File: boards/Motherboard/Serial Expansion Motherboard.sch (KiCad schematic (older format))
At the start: 5 parts, among them U401 24AA014

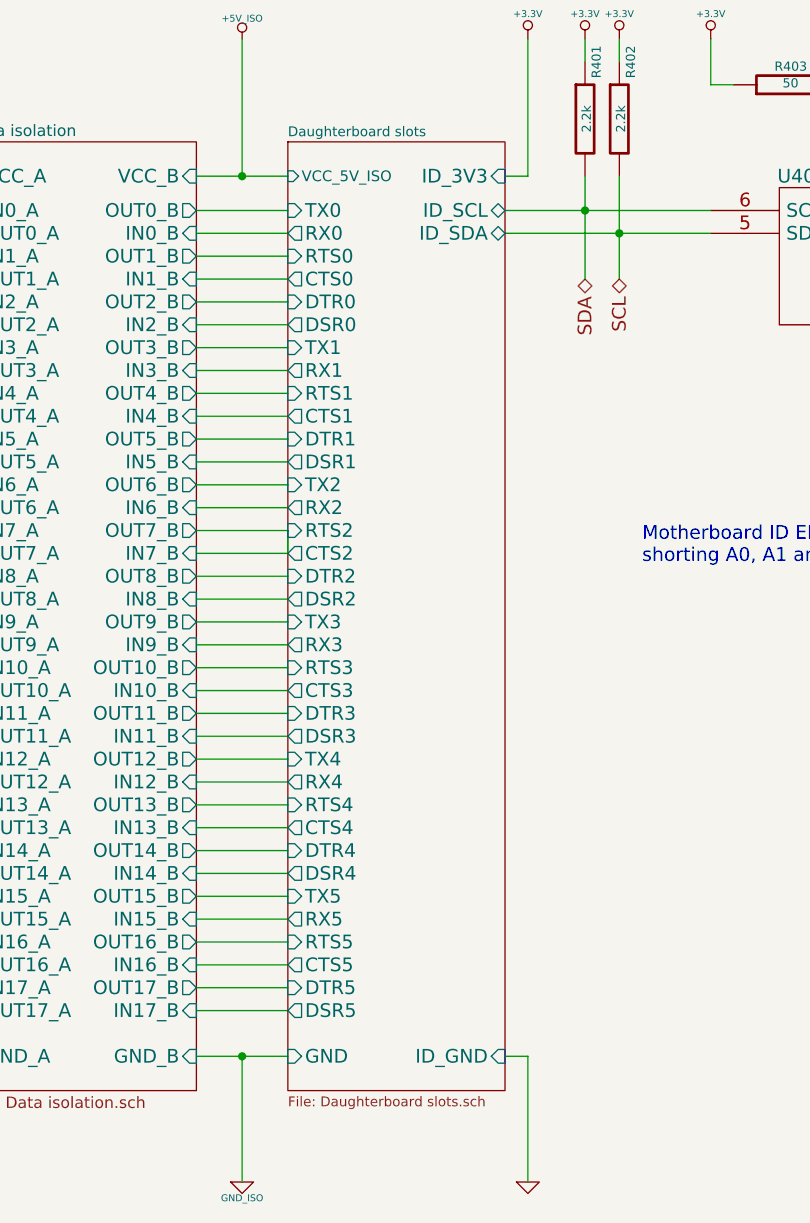
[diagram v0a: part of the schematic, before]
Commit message: Changed power pin/port names
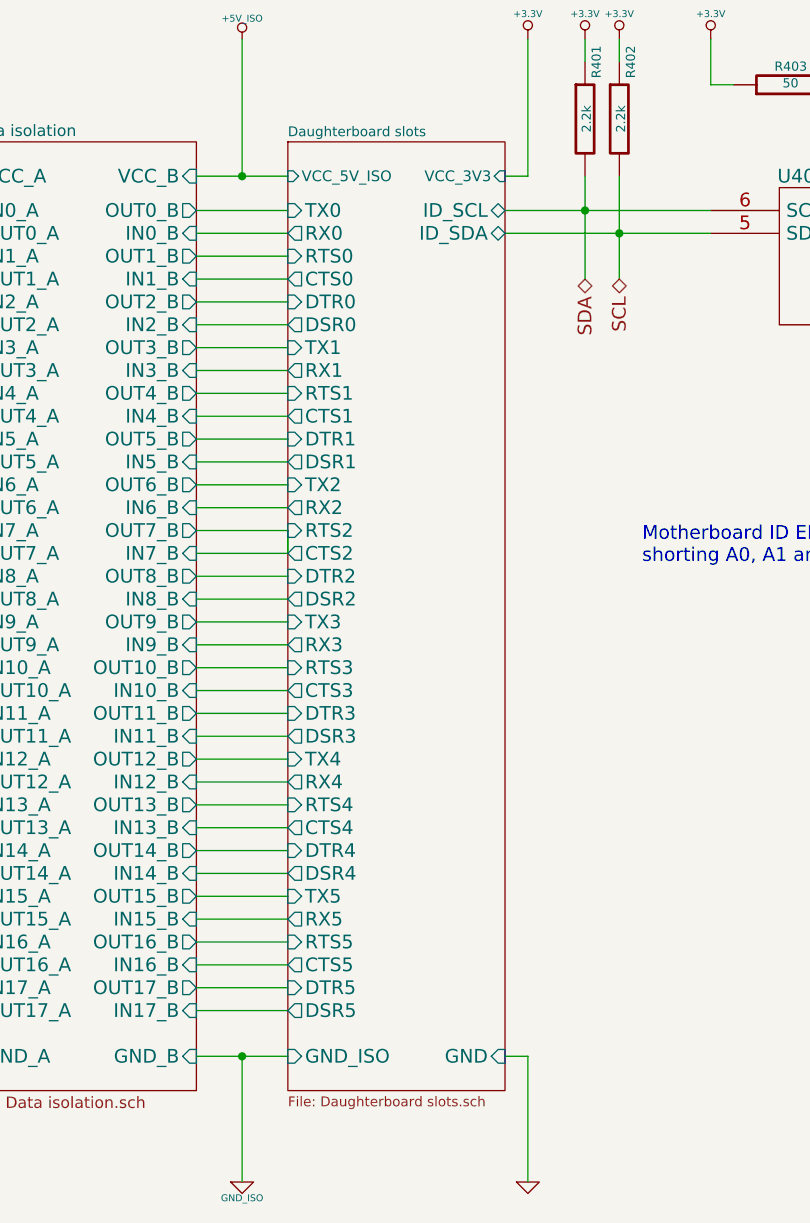
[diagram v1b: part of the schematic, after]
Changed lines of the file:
@@
 F6 "DTR0" I L 6700 2550 60
 F7 "DSR0" O L 6700 2650 60
-F8 "GND" I L 6700 5850 60
+F8 "GND_ISO" I L 6700 5850 60
 F9 "RX1" O L 6700 2850 60
 F10 "TX1" I L 6700 2750 60
@@
 F39 "ID_SDA" B R 7650 2250 60
 F40 "ID_SCL" B R 7650 2150 60
-F41 "ID_3V3" I R 7650 2000 60
-F42 "ID_GND" I R 7650 5850 60
+F41 "VCC_3V3" I R 7650 2000 47
+F42 "GND" I R 7650 5850 60
 F43 "RTS3" I L 6700 4150 60
 $EndSheet

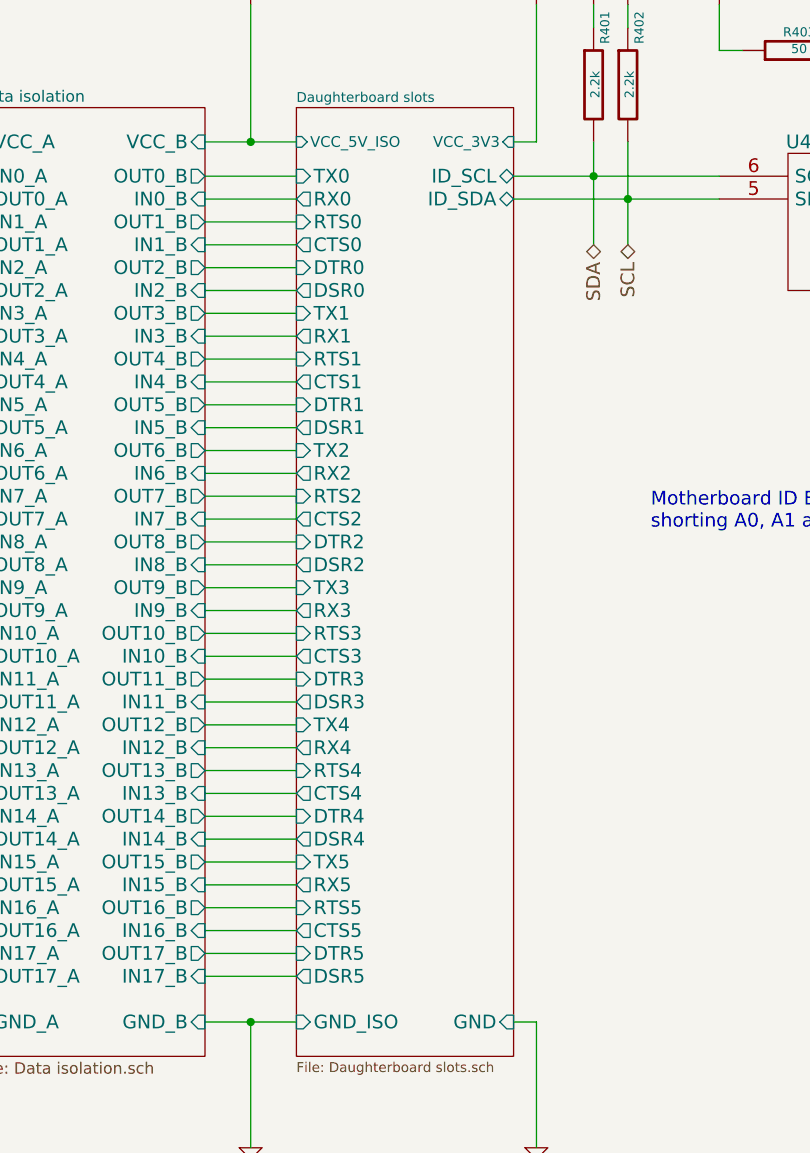
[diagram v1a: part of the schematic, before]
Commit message: Changed daughterboard slots to support Digilent PMOD and changed label names
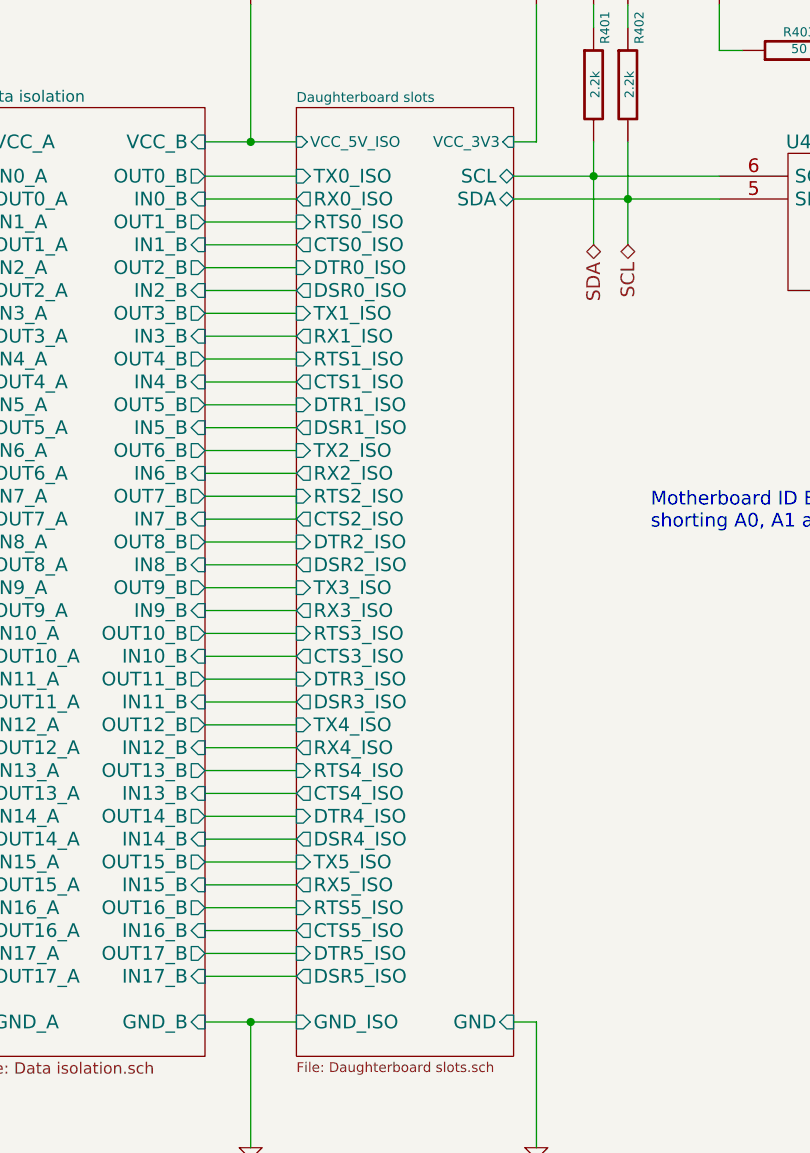
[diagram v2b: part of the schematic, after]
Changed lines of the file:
@@
 LIBS:CONN_16
 LIBS:csmall
+LIBS:dboardheader-22
 LIBS:Motherboard-cache
 EELAYER 27 0
@@
 F0 "Daughterboard slots" 43
 F1 "Daughterboard slots.sch" 43
-F2 "RX0" O L 6700 2250 60
-F3 "TX0" I L 6700 2150 60
-F4 "RTS0" I L 6700 2350 60
-F5 "CTS0" O L 6700 2450 60
-F6 "DTR0" I L 6700 2550 60
-F7 "DSR0" O L 6700 2650 60
+F2 "RX0_ISO" O L 6700 2250 60
+F3 "TX0_ISO" I L 6700 2150 60
+F4 "RTS0_ISO" I L 6700 2350 60
+F5 "CTS0_ISO" O L 6700 2450 60
+F6 "DTR0_ISO" I L 6700 2550 60
+F7 "DSR0_ISO" O L 6700 2650 60
 F8 "GND_ISO" I L 6700 5850 60
-F9 "RX1" O L 6700 2850 60
-F10 "TX1" I L 6700 2750 60
-F11 "RTS1" I L 6700 2950 60
-F12 "CTS1" O L 6700 3050 60
-F13 "DTR1" I L 6700 3150 60
-F14 "DSR1" O L 6700 3250 60
-F15 "RX2" O L 6700 3450 60
-F16 "TX2" I L 6700 3350 60
-F17 "RTS2" I L 6700 3550 60
-F18 "CTS2" O L 6700 3650 60
-F19 "DTR2" I L 6700 3750 60
-F20 "DSR2" O L 6700 3850 60
-F21 "RX3" O L 6700 4050 60
-F22 "TX3" I L 6700 3950 60
-F23 "CTS3" O L 6700 4250 60
-F24 "DTR3" I L 6700 4350 60
-F25 "DSR3" O L 6700 4450 60
-F26 "RX4" O L 6700 4650 60
-F27 "TX4" I L 6700 4550 60
-F28 "RTS4" I L 6700 4750 60
-F29 "CTS4" O L 6700 4850 60
-F30 "DTR4" I L 6700 4950 60
-F31 "DSR4" O L 6700 5050 60
-F32 "RX5" O L 6700 5250 60
-F33 "TX5" I L 6700 5150 60
-F34 "RTS5" I L 6700 5350 60
-F35 "CTS5" O L 6700 5450 60
-F36 "DTR5" I L 6700 5550 60
-F37 "DSR5" O L 6700 5650 60
+F9 "RX1_ISO" O L 6700 2850 60
+F10 "TX1_ISO" I L 6700 2750 60
+F11 "RTS1_ISO" I L 6700 2950 60
+F12 "CTS1_ISO" O L 6700 3050 60
+F13 "DTR1_ISO" I L 6700 3150 60
+F14 "DSR1_ISO" O L 6700 3250 60
+F15 "RX2_ISO" O L 6700 3450 60
+F16 "TX2_ISO" I L 6700 3350 60
+F17 "RTS2_ISO" I L 6700 3550 60
+F18 "CTS2_ISO" O L 6700 3650 60
+F19 "DTR2_ISO" I L 6700 3750 60
+F20 "DSR2_ISO" O L 6700 3850 60
+F21 "RX3_ISO" O L 6700 4050 60
+F22 "TX3_ISO" I L 6700 3950 60
+F23 "CTS3_ISO" O L 6700 4250 60
+F24 "DTR3_ISO" I L 6700 4350 60
+F25 "DSR3_ISO" O L 6700 4450 60
+F26 "RX4_ISO" O L 6700 4650 60
+F27 "TX4_ISO" I L 6700 4550 60
+F28 "RTS4_ISO" I L 6700 4750 60
+F29 "CTS4_ISO" O L 6700 4850 60
+F30 "DTR4_ISO" I L 6700 4950 60
+F31 "DSR4_ISO" O L 6700 5050 60
+F32 "RX5_ISO" O L 6700 5250 60
+F33 "TX5_ISO" I L 6700 5150 60
+F34 "RTS5_ISO" I L 6700 5350 60
+F35 "CTS5_ISO" O L 6700 5450 60
+F36 "DTR5_ISO" I L 6700 5550 60
+F37 "DSR5_ISO" O L 6700 5650 60
 F38 "VCC_5V_ISO" I L 6700 2000 47
-F39 "ID_SDA" B R 7650 2250 60
-F40 "ID_SCL" B R 7650 2150 60
+F39 "SDA" B R 7650 2250 60
+F40 "SCL" B R 7650 2150 60
 F41 "VCC_3V3" I R 7650 2000 47
 F42 "GND" I R 7650 5850 60
-F43 "RTS3" I L 6700 4150 60
+F43 "RTS3_ISO" I L 6700 4150 60
 $EndSheet
 $Comp

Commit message: Change to 5 serial port; Connect Atlys and PIC18F SPI; Entire schematic updated
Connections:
- net labels removed: CTS5, DSR5, DTR5, RTS5, RX5, TX5
- wire segments 112 -> 100

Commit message: Change all serial connections to use BUS
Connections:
- net labels added: SERIAL0, SERIAL1, SERIAL10, SERIAL11, SERIAL12, SERIAL13, SERIAL14, SERIAL15, SERIAL16, SERIAL17, SERIAL18, SERIAL19, SERIAL2, SERIAL20, SERIAL21, SERIAL22, SERIAL23, SERIAL24, SERIAL25, SERIAL26, SERIAL27, SERIAL28, SERIAL29, SERIAL3, SERIAL4, SERIAL5, SERIAL6, SERIAL7, SERIAL8, SERIAL9, SERIAL[0..29]
- wire segments 100 -> 130
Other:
- moved on the sheet: R401, R402, R403, U401
